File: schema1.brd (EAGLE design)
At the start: 115 x 59 mm, 34 parts, among them IC1 PIC16F1938SP, IC2 EXCALIBUR, IC3 LP2950CZ, X3 PG203J

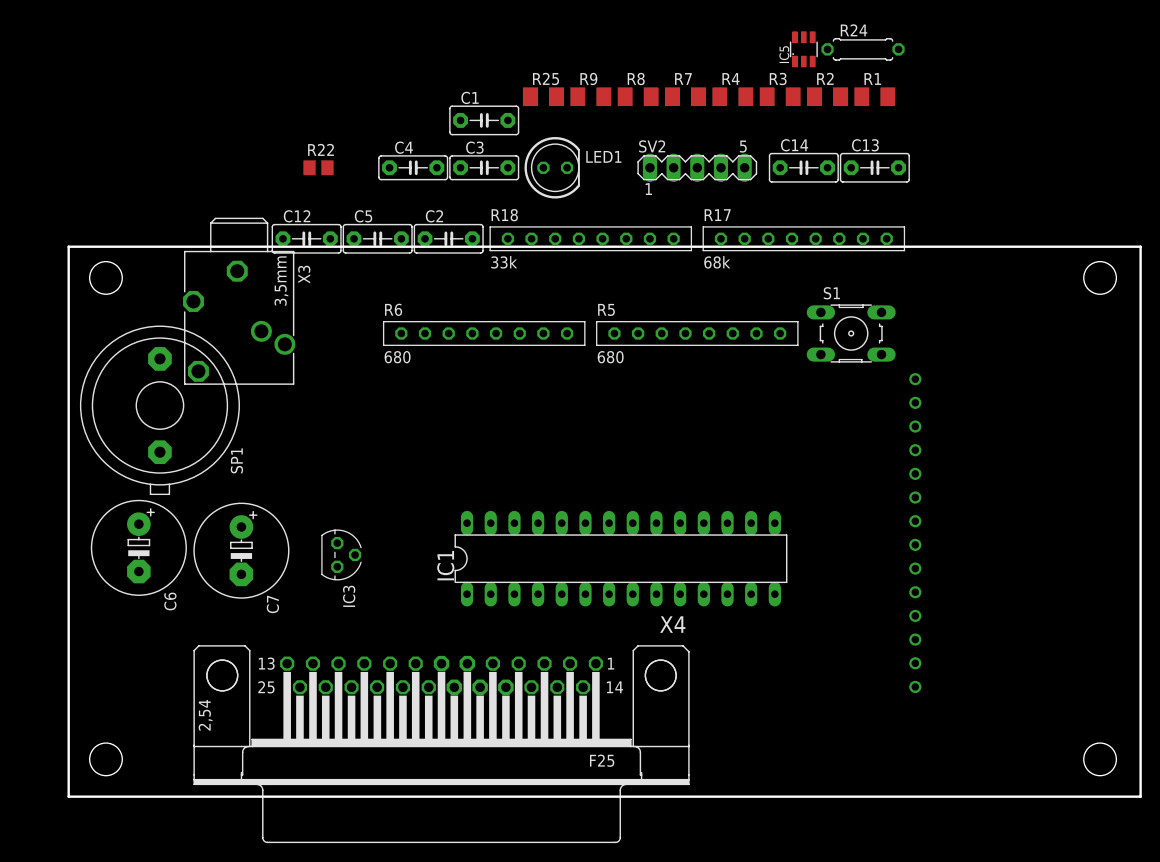
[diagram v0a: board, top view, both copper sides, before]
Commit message: Updated excalibur footprint. Updated board.
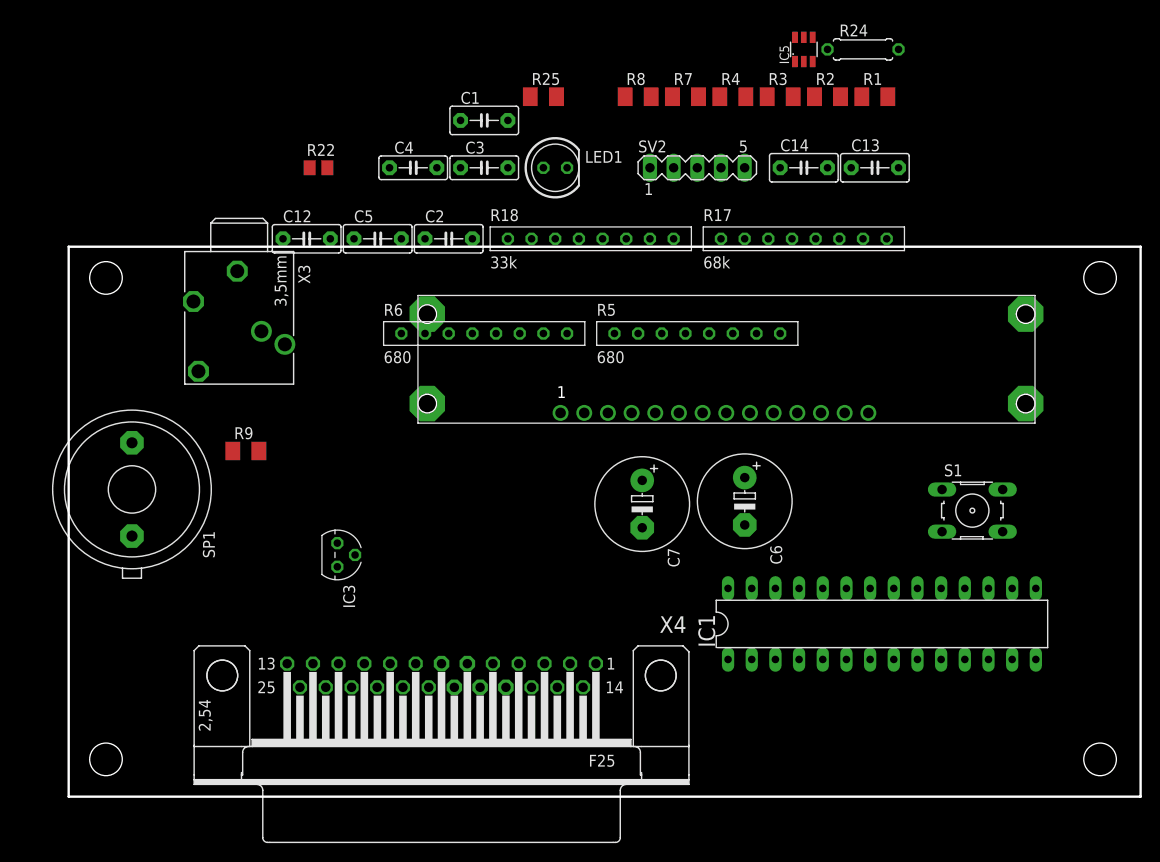
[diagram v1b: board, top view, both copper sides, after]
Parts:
- IC2: value EXCALIBUR -> (none); device julio:EXCALIBUR -> julio:TI_PKG1360
- moved C6 65.2 mm to (68.5, 27.7)
- moved R9 53.0 mm to (15.0, 33.1)
- moved IC2 48.1 mm to (48.8, 37.2), turned to 0 degrees
- moved C7 43.3 mm to (57.5, 27.4)
- moved IC1 28.9 mm to (83.2, 14.5)
- moved S1 23.0 mm to (93.0, 26.7)
- moved SP1 9.49 mm to (2.79, 29.0)

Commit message: modified:   julio.lbr 	modified:   schema1.brd 	modified:   schema1.sch
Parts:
- removed C12, C13, C14: 22n, capacitor-wima:C5B3
- removed IC5: (no value), linear-technology:TSOT23-6
- removed R17: 68k, julio:RES_ARRAY_DIP_4
- removed R18: 33k, julio:RES_ARRAY_DIP_4
- removed R22: 27k 1%, resistor:M0805
- removed R24: 787 1%, resistor:0207/7
- removed R25: 680, resistor:M1206
- removed SP1: F/EE17P, buzzer:F/EE17P
- removed SV2: (no value), con-lstb:MA05-1
- removed X4: (no value), con-subd:F25H
- added C10, C8, C9: 22n, capacitor-wima:C5B3
- added IC4: (no value), linear-technology:TSOT23-6
- added R10: 680, resistor:M1206
- added R11, R12, R14, R15: (no value), julio:RES_ARRAY_DIP_4
- added SG1, SG2: (no value), con-lstb:MA04-1
- added SV1: (no value), con-lstb:MA05-1
- added X2: (no value), con-subd:F25H
- C1: value (none) -> 22n
- C2: value 22n -> 100u; device capacitor-wima:C5B3 -> resistor:E5-10,5
- C3: value 1u -> 100u; device capacitor-wima:C5B2.5 -> resistor:E5-10,5
- C4: value 2n2 -> 1u
- C5: value 22n -> 2n2; device capacitor-wima:C5B3 -> capacitor-wima:C5B2.5
- C6: value 100u -> (none); device resistor:E5-10,5 -> capacitor-wima:C5B3
- C7: value 100u -> 22n; device resistor:E5-10,5 -> capacitor-wima:C5B3
- IC1: value PIC16F1938SP -> (none); device microchip:DIL28-3 -> julio:TI_PKG1360
- IC2: value (none) -> PIC16F1938SP; device julio:TI_PKG1360 -> microchip:DIL28-3
- LED1: device led:LED5MM -> led:CHIP-LED0805
- R1: value 270k -> 68k
- R2: value 68k -> 33k
- R3: value 33k -> 330
- R4: value 330 -> 270k
- R5: value 680 -> 787 1%; device julio:RES_ARRAY_DIP_4 -> resistor:M0805
- R6: value 680 -> 27k 1%; device julio:RES_ARRAY_DIP_4 -> resistor:M0805
- X3: value PG203J -> 1503_07; device con-hirschmann:PG203J -> con-lumberg:1503_07
- moved X3 81.9 mm to (82.8, 2.54), turned to 180 degrees
- moved IC1 74.3 mm to (15.1, 44.2)
- moved C5 55.7 mm to (83.9, 45.4), turned to 90 degrees
- moved R7 55.1 mm to (81.1, 19.3), turned to 90 degrees
- moved IC3 54.3 mm to (74.4, 44.1), turned to 180 degrees
- moved R6 53.0 mm to (83.6, 35.1), flipped to the bottom
- moved C4 50.4 mm to (80.0, 45.4), turned to 90 degrees
- moved R1 50.4 mm to (36.9, 49.6), flipped to the bottom, turned to 180 degrees
- moved LED1 50.3 mm to (86.3, 30.6), turned to 270 degrees
- moved R9 46.0 mm to (53.3, 7.59)
- moved C1 44.7 mm to (52.0, 25.4)
- moved R2 41.1 mm to (43.1, 48.3), flipped to the bottom, turned to 180 degrees
- moved R3 39.6 mm to (52.1, 37.0), flipped to the bottom, turned to 270 degrees
- moved C2 37.0 mm to (5.08, 36.8)
- moved R4 31.7 mm to (60.7, 40.1), turned to 270 degrees
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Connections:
- removed net N$10: C3.1, C6.+, IC2.P$11, IC2.P$12, IC2.P$13, IC3.3
- removed net N$11: R8.2, X4.3
- removed net N$4: IC1.14
- removed net N$5: IC1.15
- removed net VCC: C4.1, IC1.20, IC3.1, IC5.3, IC5.6, LED1.A, R1.2, SV2.2
- new net +12VR: C3.+, C4.2, IC1.P$11, IC1.P$12, IC1.P$13, IC3.3, SG2.1
- new net N$7: R9.1, X2.1
- new net SCL: IC2.14, SG2.3
- new net SDA: IC2.15, SG2.2
- new net VDD: C5.2, IC2.20, IC3.1, IC4.3, IC4.6, LED1.A, R4.1, SV1.2
- net !MCLR: now also IC2.1, R4.2, SV1.1; no longer IC1.1, R1.1, SV2.1
- net +12V: now also C2.+, IC1.P$4, IC1.P$5, IC1.P$6, R1.1, X2.12; no longer C7.+, IC2.P$4, IC2.P$5, IC2.P$6, R2.2, X4.1
- net A-ECT-I: now also R15.P$5, X2.24; no longer R6.P$7, X4.24
- net A-EXT-I: now also R12.P$1, X2.21; no longer R5.P$1, X4.9
- net A-FL-I: now also R12.P$5, X2.22; no longer R5.P$3, X4.10
- net A-HO2-I: now also R15.P$3, X2.11; no longer R6.P$5, X4.23
- net A-IAT-I: now also R12.P$3, X2.9; no longer R5.P$5, X4.11
- net A-MAP-I: now also R12.P$7, X2.10; no longer R5.P$7, X4.21
- net A-TPS-I: now also R15.P$1, X2.23; no longer R6.P$3, X4.22
- net ALT: now also C9.2, IC2.16, R11.P$6, R14.P$5; no longer C13.1, IC1.16, R17.P$6, R18.P$5
- net ALT_1: now also R11.P$5, X2.4; no longer R17.P$5, X4.16
- net BAT: now also C1.2, IC2.6, R3.2; no longer C5.1, IC1.6, R4.2
- net BEEP: now also IC2.24, R8.2; no longer IC1.24, R9.2
- net CKP: now also IC2.13, R10.2; no longer IC1.13, R7.1
- net DGND: now also C1.1, C10.1, C2.-, C3.-, C4.1, C5.1, C6.2, C7.1, C8.2, C9.1, IC1.P$10, IC1.P$7, IC1.P$8, IC1.P$9, IC2.19, IC2.8, IC4.2, R14.P$2, R14.P$4, R14.P$6, R14.P$8, R2.1, R5.2, R7.1, SG1.4, SG2.4, SV1.3, X2.18, X2.5; no longer C1.2, C12.2, C13.2, C14.2, C2.2, C3.2, C4.2, C5.2, C6.-, C7.-, IC1.19, IC1.8, IC2.P$10, IC2.P$7, IC2.P$8, IC2.P$9, IC5.2, R18.P$2, R18.P$4, R18.P$6, R18.P$8, R24.1, R25.1, R3.1, SP1.2, SV2.3, X4.18, X4.5
- net ECT: now also IC2.2, R15.P$6; no longer IC1.2, R6.P$8
- net EXT: now also IC2.26, R12.P$2; no longer IC1.26, R5.P$2
- net FAN: now also C10.2, IC2.10, R11.P$8, R14.P$7; no longer C14.1, IC1.10, R17.P$8, R18.P$7
- net FAN_1: now also R11.P$7, X2.17; no longer R17.P$7, X4.4
- net FLV: now also C6.1, IC2.23, R12.P$6; no longer C1.1, IC1.23, R5.P$4
- net HO2: now also IC2.3, R15.P$4; no longer IC1.3, R6.P$6
- net IAT: now also IC2.7, R12.P$4; no longer IC1.7, R5.P$6
- net ICSPCLK: now also IC2.27, SV1.5; no longer IC1.27, SV2.5
- net ICSPDAT: now also IC2.28, SV1.4; no longer IC1.28, SV2.4
- net MAP: now also IC2.25, R12.P$8; no longer IC1.25, R5.P$8
- net N$1: now also R8.1, SG1.1; no longer R9.1, SP1.1
- net N$2: now also IC4.4, R6.1; no longer IC5.4, R22.2
- net N$3: now also LED1.C, R7.2; no longer LED1.K, R25.2
- net N$6: now also R5.1, R6.2; no longer R22.1, R24.2
- net N$8: now also R1.2, R2.2, R3.1; no longer R2.1, R3.2, R4.1
- net N$9: now also R10.1, X2.14; no longer R7.2, X4.2
- net PCS: now also C8.1, IC2.22, R11.P$4, R14.P$3; no longer C12.1, IC1.22, R17.P$4, R18.P$3
- net PCS_1: now also R11.P$3, X2.16; no longer R17.P$3, X4.17
- net T1CKI: now also IC2.11, IC4.1; no longer IC1.11, IC5.1
- net TPS: now also IC2.21, R15.P$2; no longer IC1.21, R6.P$4
- net UART_RX: now also IC2.18, X3.2@1; no longer IC1.18, X3.2
- net UART_TX: now also IC2.17, X3.3; no longer IC1.17, X3.5
- net VREF+: now also IC2.5, X2.6; no longer IC1.5, X4.8
- net VREF-: now also IC2.4, X2.7; no longer IC1.4, X4.7
- net VSS: now also IC2.12, R9.2; no longer IC1.12, R8.1
- net VTS: now also C7.2, IC2.9, R11.P$2, R14.P$1; no longer C2.1, IC1.9, R17.P$2, R18.P$1
- net VTS_1: now also R11.P$1, X2.3; no longer R17.P$1, X4.15
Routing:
- net DGND: track 0.00 -> 319.6 mm
- net +12VR: track 0.00 -> 110.6 mm
- net VDD: track 0.00 -> 101.9 mm
- net SDA: track 0.00 -> 92.3 mm
- net SCL: track 0.00 -> 79.6 mm
- net EXT: track 0.00 -> 72.6 mm
- net VREF-: track 0.00 -> 69.5 mm, vias 0 -> 1
- net VREF+: track 0.00 -> 67.1 mm, vias 0 -> 1
- net TPS: track 0.00 -> 65.5 mm
- net +12V: track 0.00 -> 65.4 mm
- net HO2: track 0.00 -> 64.3 mm
- net ALT: track 0.00 -> 62.8 mm
- net ECT: track 0.00 -> 60.0 mm
- net FLV: track 0.00 -> 59.8 mm
- net MAP: track 0.00 -> 58.1 mm
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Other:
- board size 115 x 59 mm -> 6.8 x 10.3 mm
